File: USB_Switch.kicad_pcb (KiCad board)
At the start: 2 copper layers, 42 x 61 mm, 30 parts, among them J1 Conn_01x06, J2 USB_IN, J3 USB_OUT, J4 Conn_01x08, J5 USB_OUT, Q1 Q_NMOS_GDS, Q2 Q_NMOS_GDS, SW1 PRGM, U1 AMS1117-3.3, U2 INA219AxD, U3 INA219AxD, U4 ESP-12F

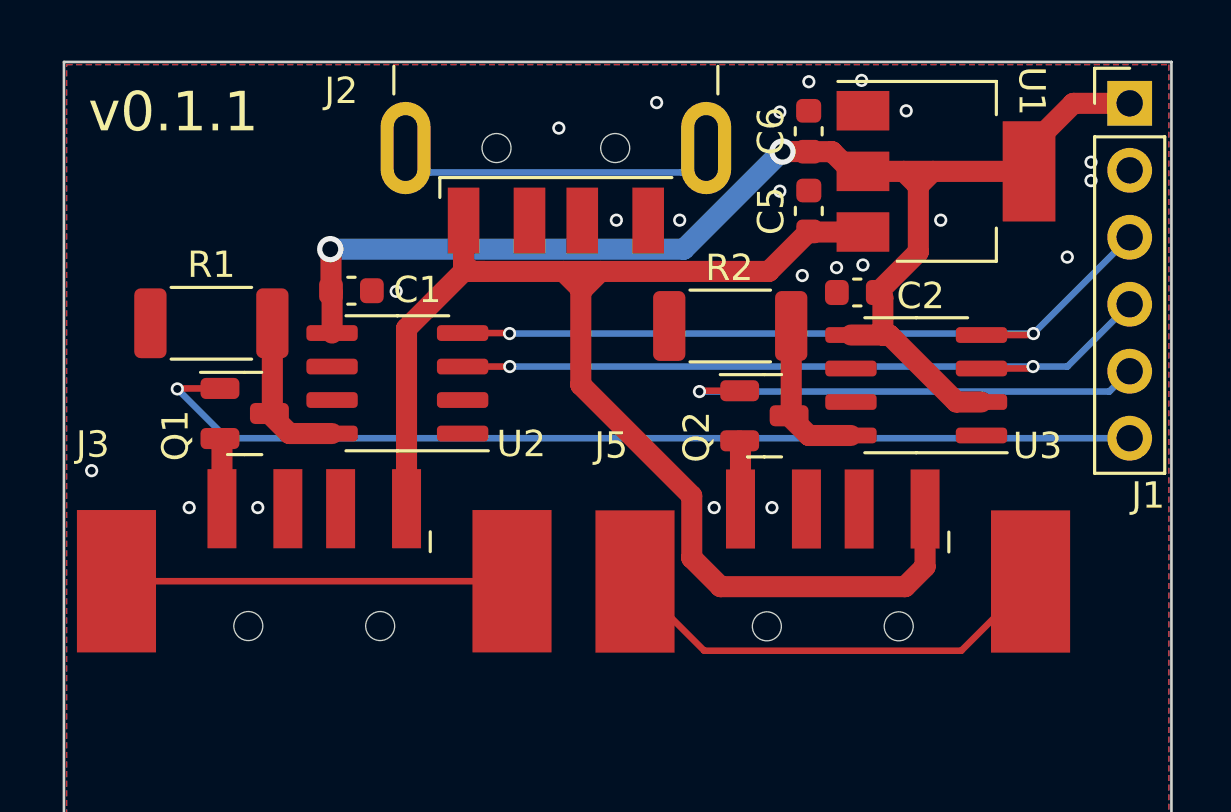
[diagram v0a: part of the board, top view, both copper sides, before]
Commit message: Updated footprints, fixed PCB layout
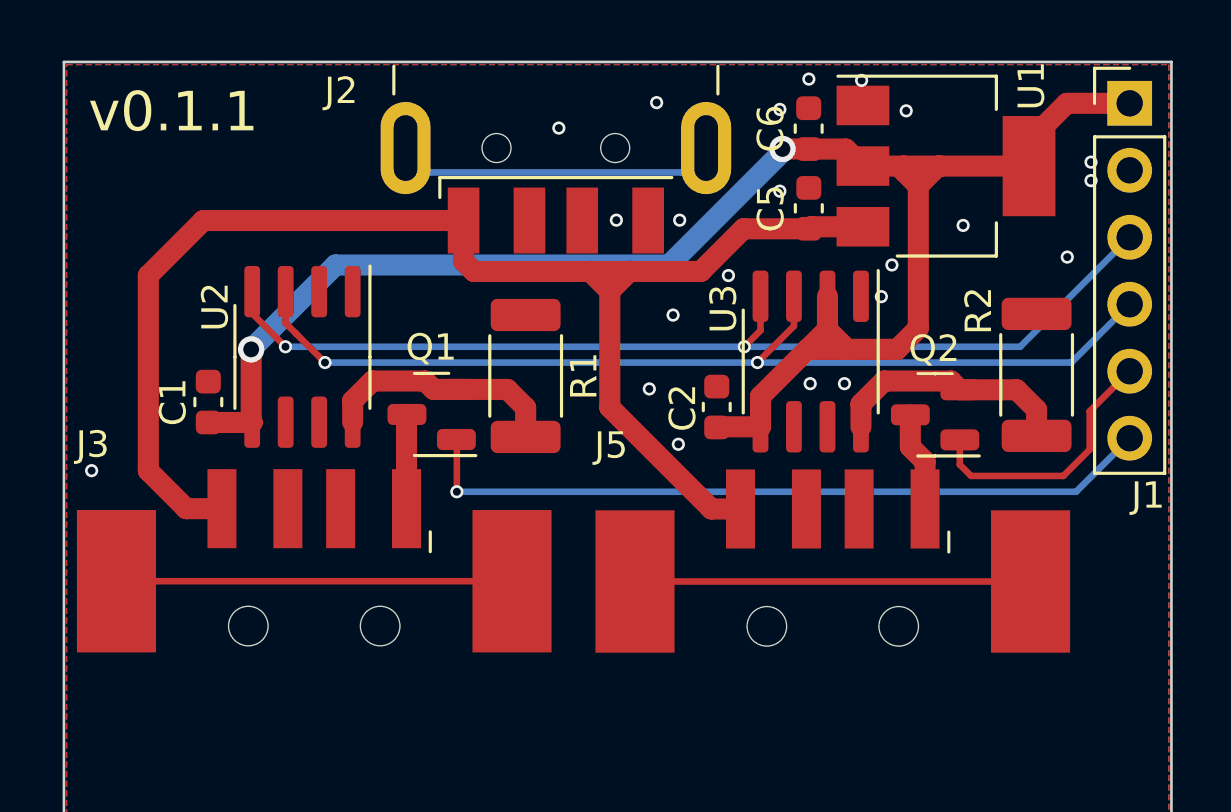
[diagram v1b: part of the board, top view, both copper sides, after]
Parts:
- moved R1 12.1 mm to (53.0, 94.2), turned to 90 degrees
- moved R2 11.8 mm to (72.4, 94.2), turned to 90 degrees
- moved Q1 7.09 mm to (49.5, 95.7), turned to 180 degrees
- moved C1 6.88 mm to (41.0, 95.2), turned to 90 degrees
- moved C2 6.88 mm to (60.3, 95.4), turned to 90 degrees
- moved Q2 6.47 mm to (68.6, 95.7), turned to 180 degrees
- moved U3 4.10 mm to (63.9, 93.7), turned to -90 degrees
- moved U2 3.74 mm to (44.6, 93.5), turned to -90 degrees
- moved U1 0.20 mm to (69.0, 86.3)
- moved C5 0.10 mm to (63.8, 87.9)
- moved C6 0.10 mm to (63.8, 84.9)
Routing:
- net /MOSFET Board/M_3v3: track 50.9 -> 63.6 mm
- net /MOSFET Board/M1_TOGGLE: track 38.5 -> 28.3 mm
- net /MOSFET Board/M_I2C_SCL: track 28.8 -> 38.5 mm
- net /MOSFET Board/M_I2C_SDA: track 28.3 -> 37.8 mm
- net /MOSFET Board/M2_TOGGLE: track 18.2 -> 10.1 mm, vias 1 -> 0
- net /MOSFET Board/5V_PRER_2: track 6.09 -> 9.33 mm
- net /MOSFET Board/5V_PRER_1: track 6.16 -> 9.21 mm
- net unconnected-(J5-Pad5): track 17.2 -> 15.0 mm
- net /MOSFET Board/SW_GND_2: track 2.60 -> 3.80 mm
- net /MOSFET Board/SW_GND_1: track 2.69 -> 3.58 mm

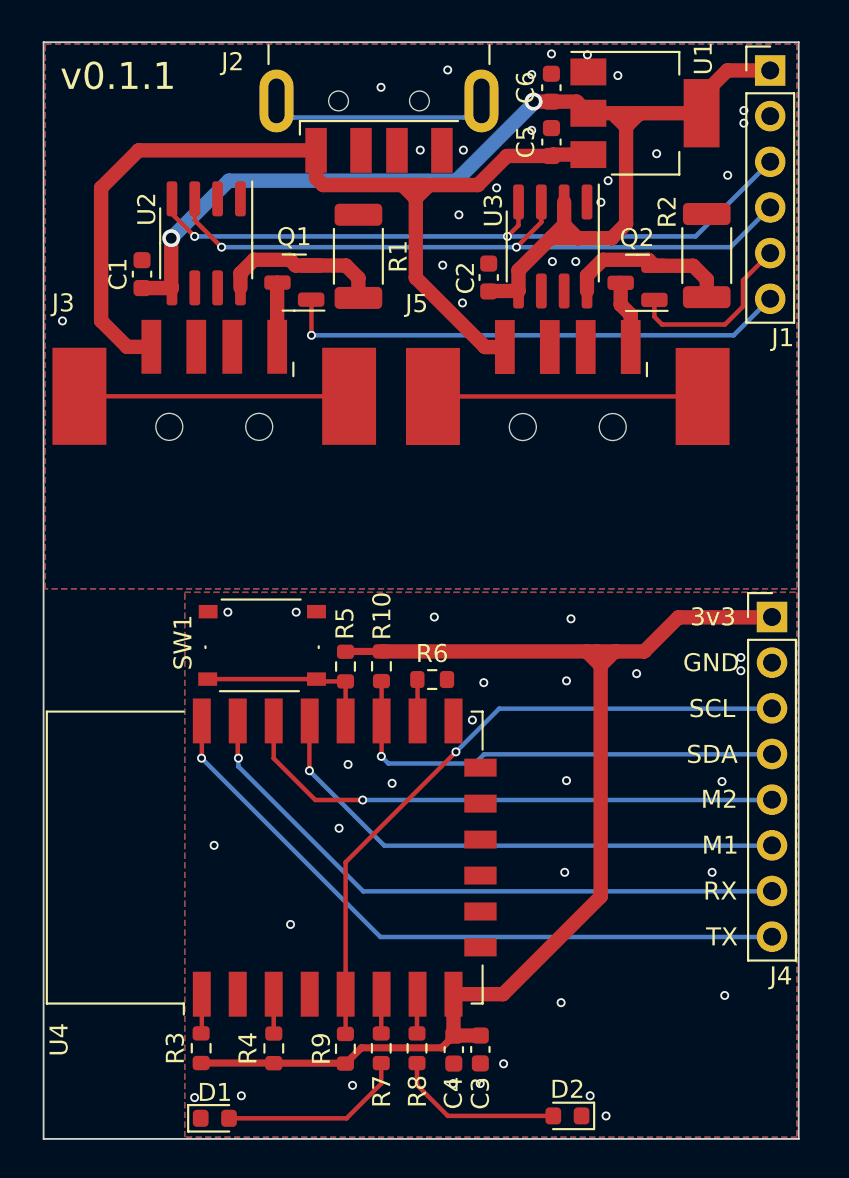
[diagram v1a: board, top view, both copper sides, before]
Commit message: Updated version number, added to second half of board
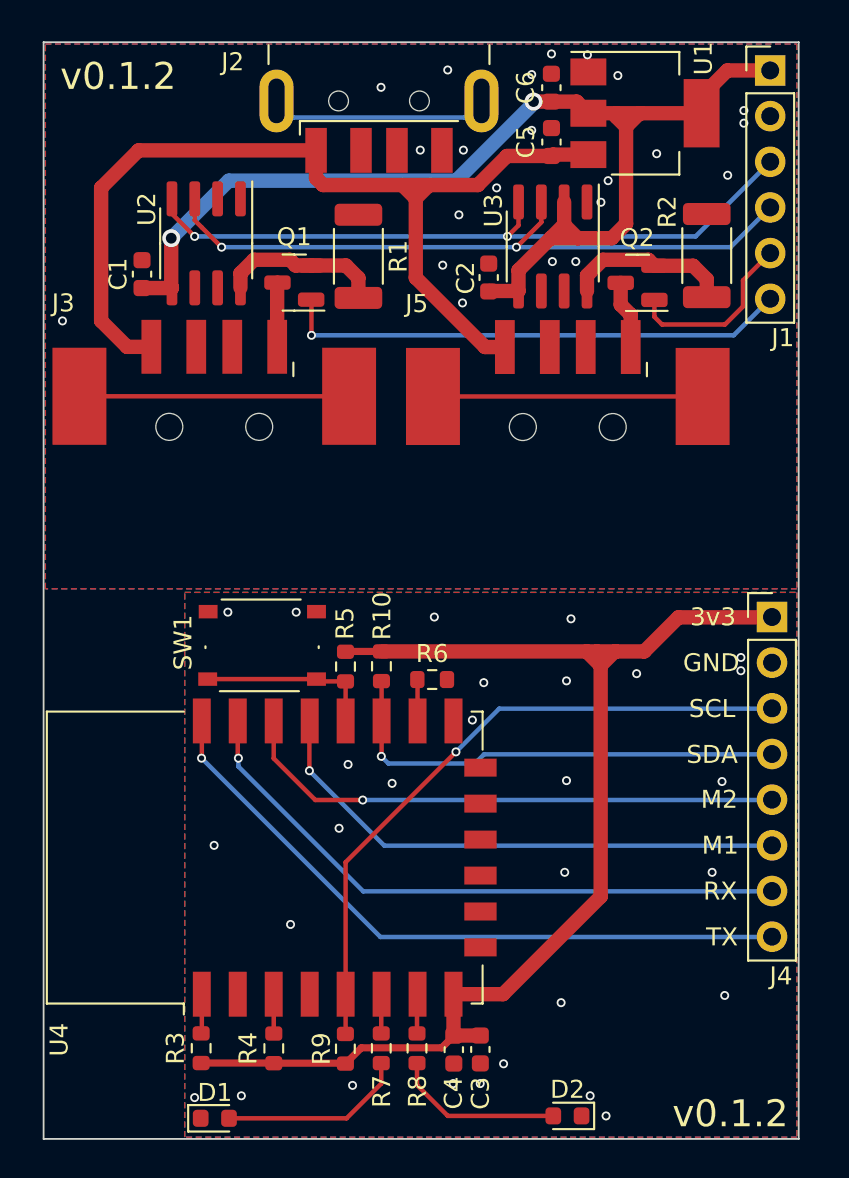
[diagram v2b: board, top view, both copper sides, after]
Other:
- board text added: "v0.1.2"
- board text removed: "v0.1.1"
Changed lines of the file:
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@@
     (effects (font (size 1 1) (thickness 0.15)) (justify mirror))
+  )
+  (gr_text "v0.1.2" (at 73.7336 141.9304) (layer "F.SilkS")
+    (effects (font (size 1.5 1.5) (thickness 0.3)))
   )
   (gr_text "TX" (at 73.268794 132.101606) (layer "F.SilkS")
@@
     (effects (font (size 1 1) (thickness 0.15)))
   )
-  (gr_text "v0.1.1" (at 39.6836 84.2304) (layer "F.SilkS")
+  (gr_text "v0.1.2" (at 39.6836 84.2304) (layer "F.SilkS")
     (effects (font (size 1.5 1.5) (thickness 0.3)))
   )

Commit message: Updated to v0.2.0
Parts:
- moved SW1 108.4 mm to (155.2, 102.1), turned to 90 degrees
- moved R8 97.5 mm to (152.9, 125.2)
- moved C5 96.7 mm to (159.3, 73.3), turned to 180 degrees
- moved C2 96.5 mm to (154.9, 76.7), turned to -90 degrees
- moved C1 96.4 mm to (135.6, 76.7), turned to -90 degrees
- moved D1 94.5 mm to (138.2, 126.0)
- moved C6 93.9 mm to (157.0, 74.1), turned to -90 degrees
- moved J2 93.8 mm to (146.1, 59.7)
- moved J3 93.1 mm to (136.4, 83.3)
- moved R10 92.9 mm to (145.8, 100.6)
- moved R5 92.9 mm to (143.8, 100.6)
- moved R6 92.9 mm to (148.6, 101.3)
- moved R9 92.9 mm to (143.8, 121.9)
- moved U4 92.8 mm to (139.2, 111.3)
- moved R4 92.8 mm to (139.7, 121.9)
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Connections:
- net /MOSFET Board/SW_GND_1 renamed /MOSFET Board/Switch Circuit/PRE_MOS
- net /MOSFET Board/SW_GND_2 renamed /MOSFET Board/Switch Circuit1/PRE_MOS
- J3 pad 1: /MOSFET Board/5V_IN -> /MOSFET Board/Switch Circuit/POST_RES
- J5 pad 1: /MOSFET Board/5V_IN -> /MOSFET Board/Switch Circuit1/POST_RES
- Q1 pad 3: /MOSFET Board/5V_PRER_1 -> GND
- Q2 pad 3: /MOSFET Board/5V_PRER_2 -> GND
- R1 pad 1: /MOSFET Board/5V_PRER_1 -> /MOSFET Board/5V_IN
- R1 pad 2: GND -> /MOSFET Board/Switch Circuit/POST_RES
- R2 pad 1: /MOSFET Board/5V_PRER_2 -> /MOSFET Board/5V_IN
- R2 pad 2: GND -> /MOSFET Board/Switch Circuit1/POST_RES
- U2 pad 7: GND -> /MOSFET Board/Switch Circuit/POST_RES
- U2 pad 8: /MOSFET Board/5V_PRER_1 -> /MOSFET Board/5V_IN
- U3 pad 7: GND -> /MOSFET Board/Switch Circuit1/POST_RES
- U3 pad 8: /MOSFET Board/5V_PRER_2 -> /MOSFET Board/5V_IN
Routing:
- net /MOSFET Board/M_3v3: track 63.6 -> 50.4 mm, vias 2 -> 0
- net /MOSFET Board/Switch Circuit1/POST_RES: track 0.00 -> 9.87 mm
- net /MOSFET Board/Switch Circuit/POST_RES: track 0.00 -> 9.87 mm
- net /MOSFET Board/5V_PRER_2: track 9.33 -> 0.00 mm
- net /MOSFET Board/5V_PRER_1: track 9.21 -> 0.00 mm
- net Net-(R5-Pad1): track 9.92 -> 19.0 mm
- net Net-(D1-Pad2): track 10.3 -> 1.52 mm
- net /Control Board/LED_2: track 2.20 -> 10.9 mm, vias 0 -> 2
- net /Control Board/LED_1: track 2.19 -> 10.3 mm, vias 0 -> 2
- net Net-(D2-Pad2): track 9.36 -> 1.52 mm
- net /MOSFET Board/M2_TOGGLE: track 10.1 -> 3.80 mm
- net /Control Board/M1_TOGGLE: track 30.2 -> 35.9 mm, vias 1 -> 0
- net /MOSFET Board/M1_TOGGLE: track 28.3 -> 23.0 mm
- net /Control Board/C_3v3: track 68.6 -> 63.3 mm, vias 0 -> 2
- net /Control Board/C_TX: track 37.9 -> 33.7 mm, vias 1 -> 0
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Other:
- board size 42 x 61 mm -> 38.1 x 63.5 mm
- board text added: "v0.2.0"
- board text removed: "v0.1.2"

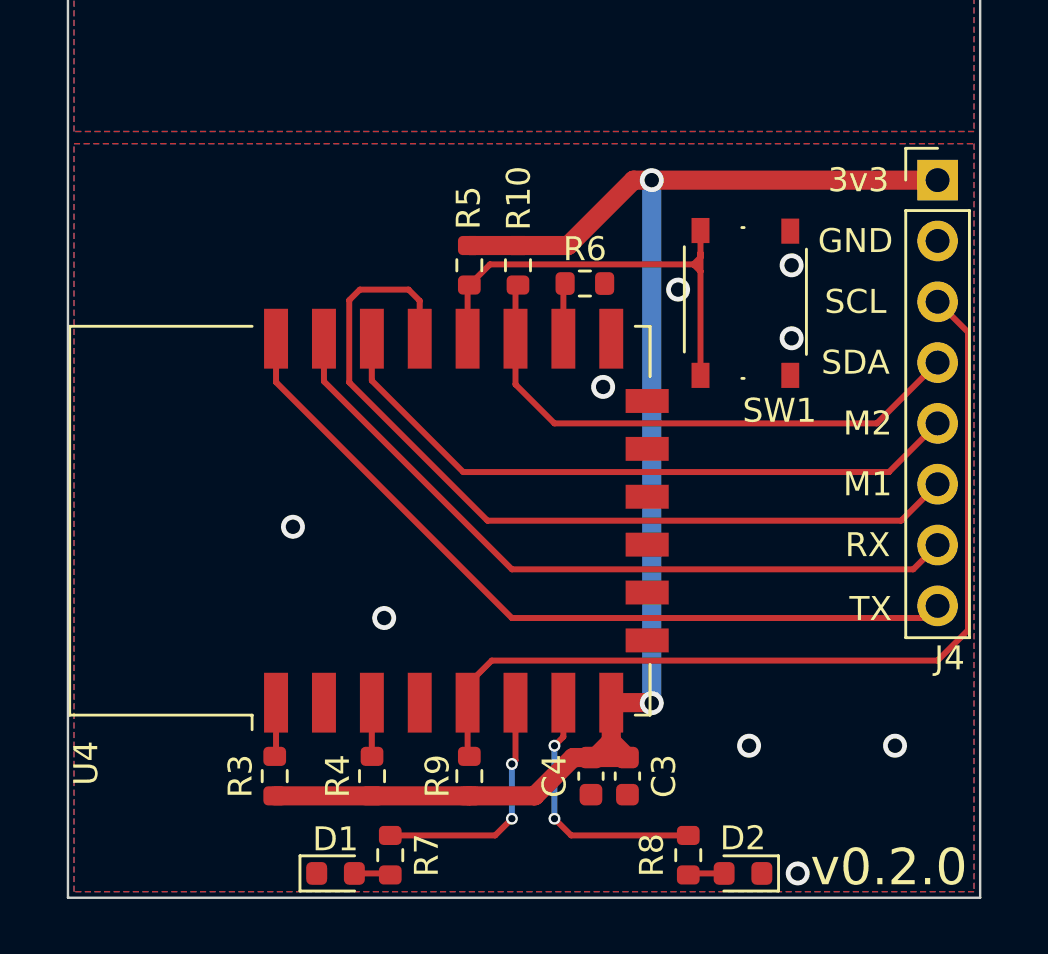
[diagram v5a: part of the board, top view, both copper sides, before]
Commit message: Removed rule zone, changed copper pour region
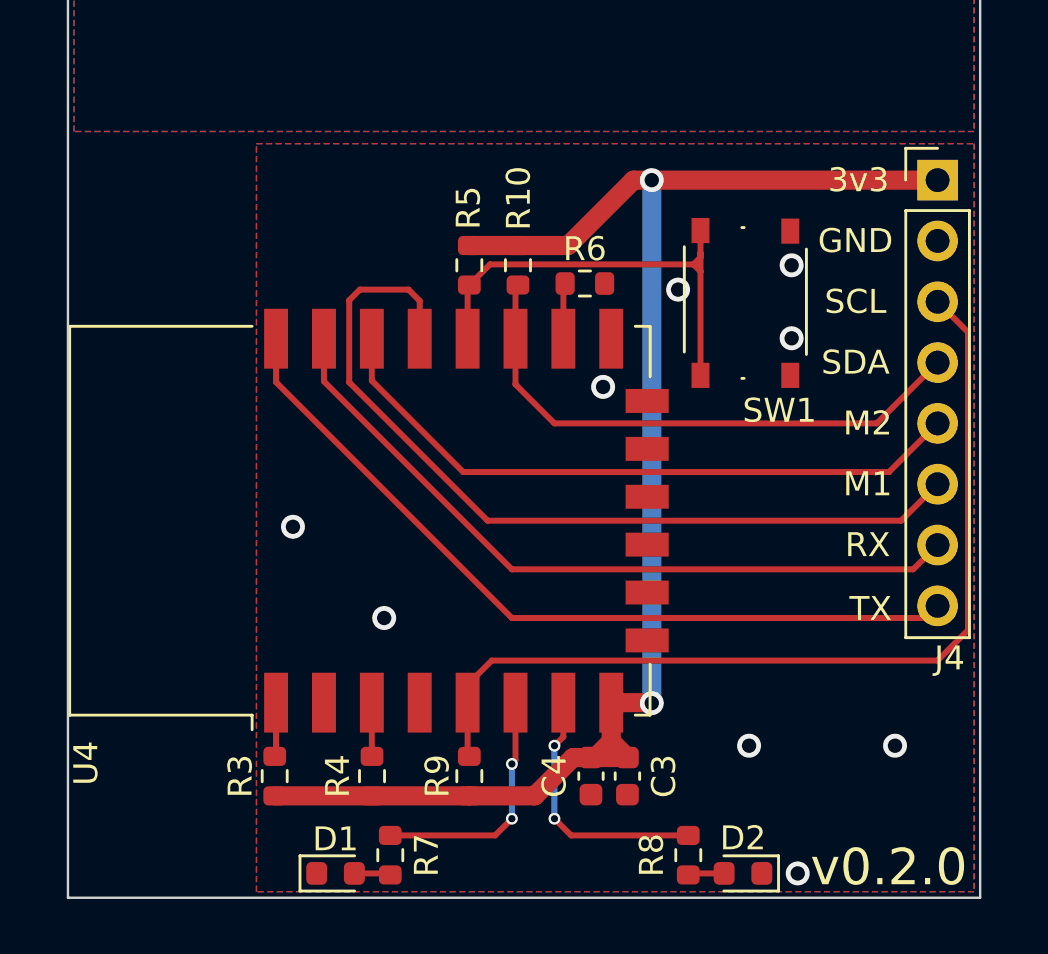
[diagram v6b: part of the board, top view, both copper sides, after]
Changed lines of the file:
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@@
       (pts
         (xy 164.846 126.746)
-        (xy 127.254 126.746)
-        (xy 127.254 95.504)
+        (xy 134.874 126.746)
+        (xy 134.874 95.504)
         (xy 164.846 95.504)
       )
@@
       )
     )
-  )
-  (zone (net 0) (net_name "") (layers F&B.Cu) (name "Antenna") (hatch edge 0.508)
-    (connect_pads (clearance 0))
-    (min_thickness 0.254)
-    (keepout (tracks not_allowed) (vias not_allowed) (pads not_allowed ) (copperpour not_allowed) (footprints allowed))
-    (fill (thermal_gap 0.508) (thermal_bridge_width 0.508))
-    (polygon
-      (pts
-        (xy 134.874 120.142)
-        (xy 127 120.142)
-        (xy 127 102.362)
-        (xy 134.874 102.362)
-      )
-    )
